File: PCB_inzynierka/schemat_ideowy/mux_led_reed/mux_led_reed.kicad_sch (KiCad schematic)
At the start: 70 parts, among them J1 Conn_01x01_Pin, J2 Conn_01x03_Pin, J3 Conn_01x01_Pin, J4 Conn_01x03_Pin, SW1 SW_Reed, SW10 SW_Reed, SW11 SW_Reed, SW12 SW_Reed, SW13 SW_Reed, SW14 SW_Reed, SW15 SW_Reed, SW16 SW_Reed, SW2 SW_Reed, SW3 SW_Reed, SW4 SW_Reed, SW5 SW_Reed, SW6 SW_Reed, SW7 SW_Reed, SW8 SW_Reed, SW9 SW_Reed, U1 74HC4051D_653, U2 74HC4051D_653

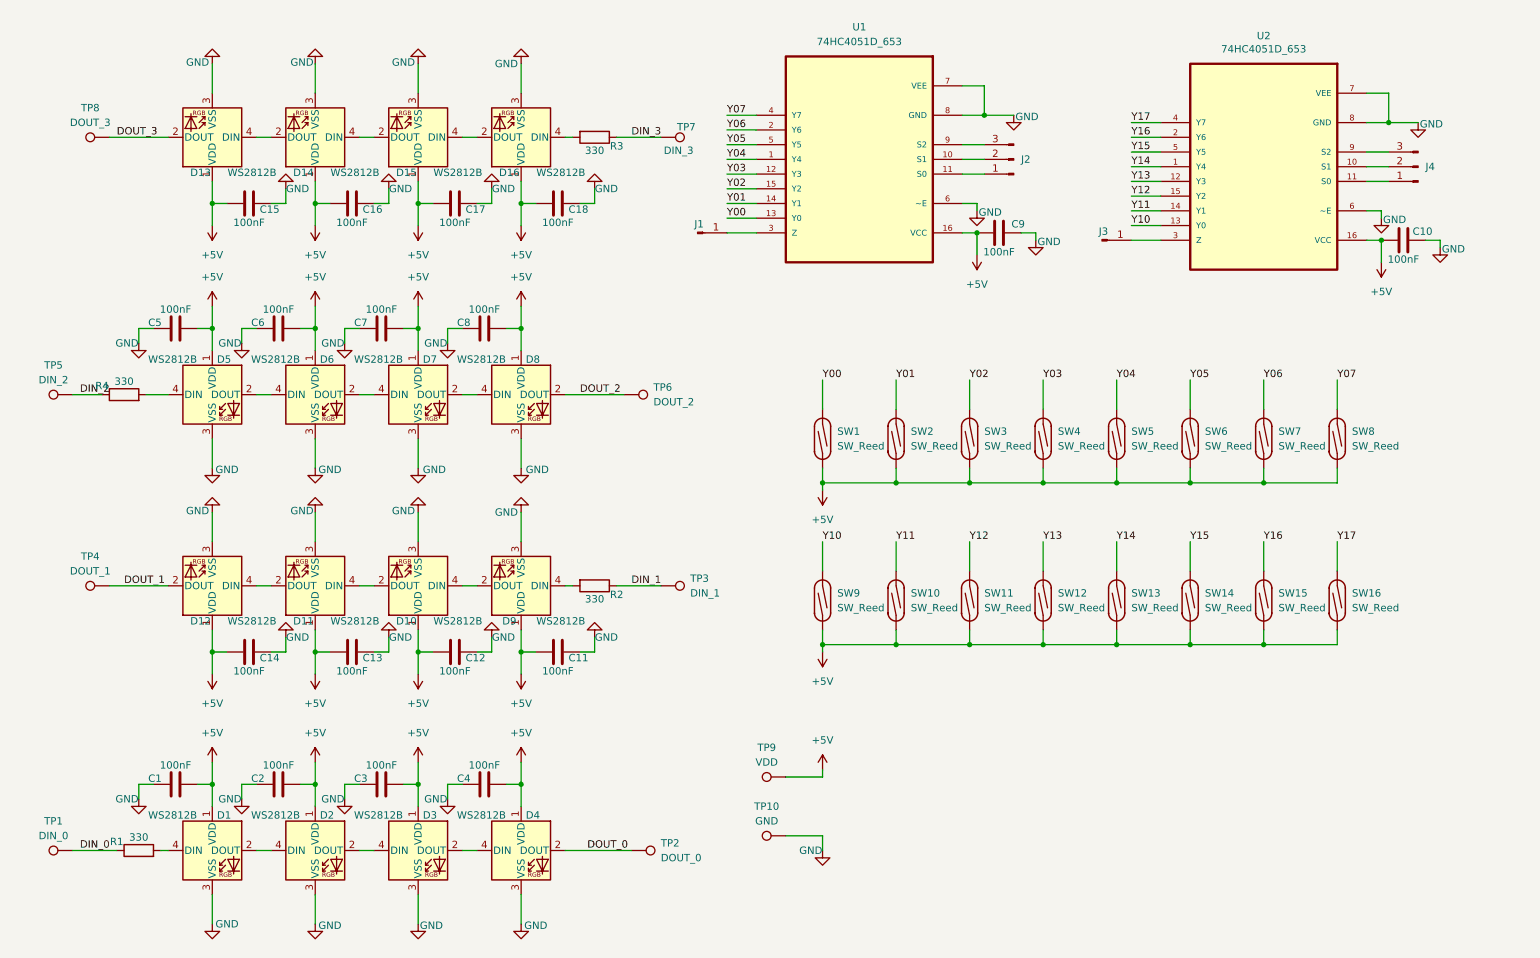
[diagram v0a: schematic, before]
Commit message: first version of 4x4 pcb for chessboard
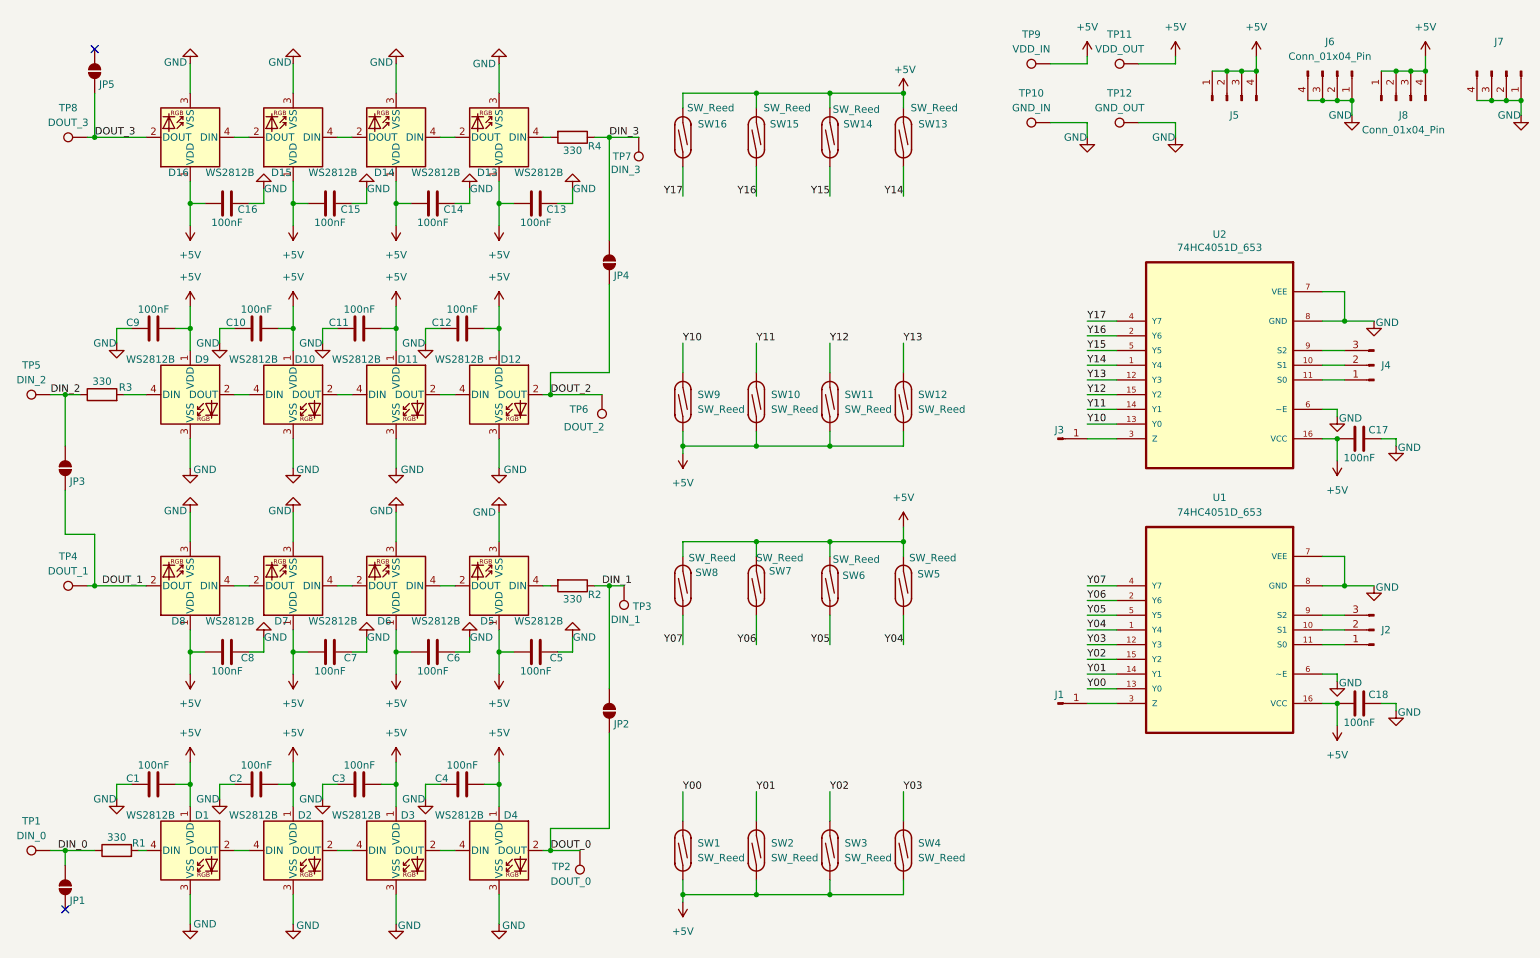
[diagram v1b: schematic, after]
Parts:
- added J5, J6: Conn_01x04_Pin, Connector_PinHeader_2.54mm:PinHeader_1x04_P2.54mm_Horizontal, symbol Connector:Conn_01x04_Pin
- added J7, J8: Conn_01x04_Pin, Connector_PinSocket_2.54mm:PinSocket_1x04_P2.54mm_Horizontal, symbol Connector:Conn_01x04_Pin
- added JP1, JP2, JP3, JP4, JP5: SolderJumper_2_Open, Jumper:SolderJumper-2_P1.3mm_Open_Pad1.0x1.5mm, symbol Jumper:SolderJumper_2_Open
- added TP11: VDD_OUT, TestPoint:TestPoint_Pad_4.0x4.0mm, symbol Connector:TestPoint
- added TP12: GND_OUT, TestPoint:TestPoint_Pad_4.0x4.0mm, symbol Connector:TestPoint
- J1, J3: footprint Connector_PinHeader_2.00mm:PinHeader_1x01_P2.00mm_Vertical -> Connector_PinHeader_2.54mm:PinHeader_1x01_P2.54mm_Vertical
- TP1, TP2, TP3, TP4, TP5, TP6, TP7, TP8: footprint TestPoint:TestPoint_Pad_4.0x4.0mm -> TestPoint:TestPoint_Pad_3.0x3.0mm
- TP10: value GND -> GND_IN
- TP9: value VDD -> VDD_IN
- renumbered C6 to C10, C7 to C11, C8 to C12, C18 to C13, C17 to C14, C16 to C15, C15 to C16, C10 to C17, C9 to C18, C11 to C5, C12 to C6, C13 to C7, C14 to C8, C5 to C9, D6 to D10, D7 to D11, D8 to D12, D16 to D13, D15 to D14, D14 to D15, D13 to D16, D9 to D5, D10 to D6, D11 to D7, D12 to D8, D5 to D9, R4 to R3, R3 to R4
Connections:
- net +5V: now also J5.1 (Pin_1), J5.2 (Pin_2), J5.3 (Pin_3), J5.4 (Pin_4), J8.1 (Pin_1), J8.2 (Pin_2), J8.3 (Pin_3), J8.4 (Pin_4), TP11.1
- net DIN_0: now also JP1.2 (B)
- net DIN_1: now also JP2.2 (B)
- net DIN_2: now also JP3.2 (B)
- net DIN_3: now also JP4.2 (B)
- net DOUT_0: now also JP2.1 (A)
- net DOUT_1: now also JP3.1 (A)
- net DOUT_2: now also JP4.1 (A)
- net DOUT_3: now also JP5.1 (A)
- net GND: now also J6.1 (Pin_1), J6.2 (Pin_2), J6.3 (Pin_3), J6.4 (Pin_4), J7.1 (Pin_1), J7.2 (Pin_2), J7.3 (Pin_3), J7.4 (Pin_4), TP12.1
- no-connect marks 0 -> 2
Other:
- moved on the sheet: C1, C10, C11, C12, C13, C14, C15, C16, C17, C18, C2, C3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

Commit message: plytka 4x4 zawierajaca mux, reed switche i ledy argb v1.0
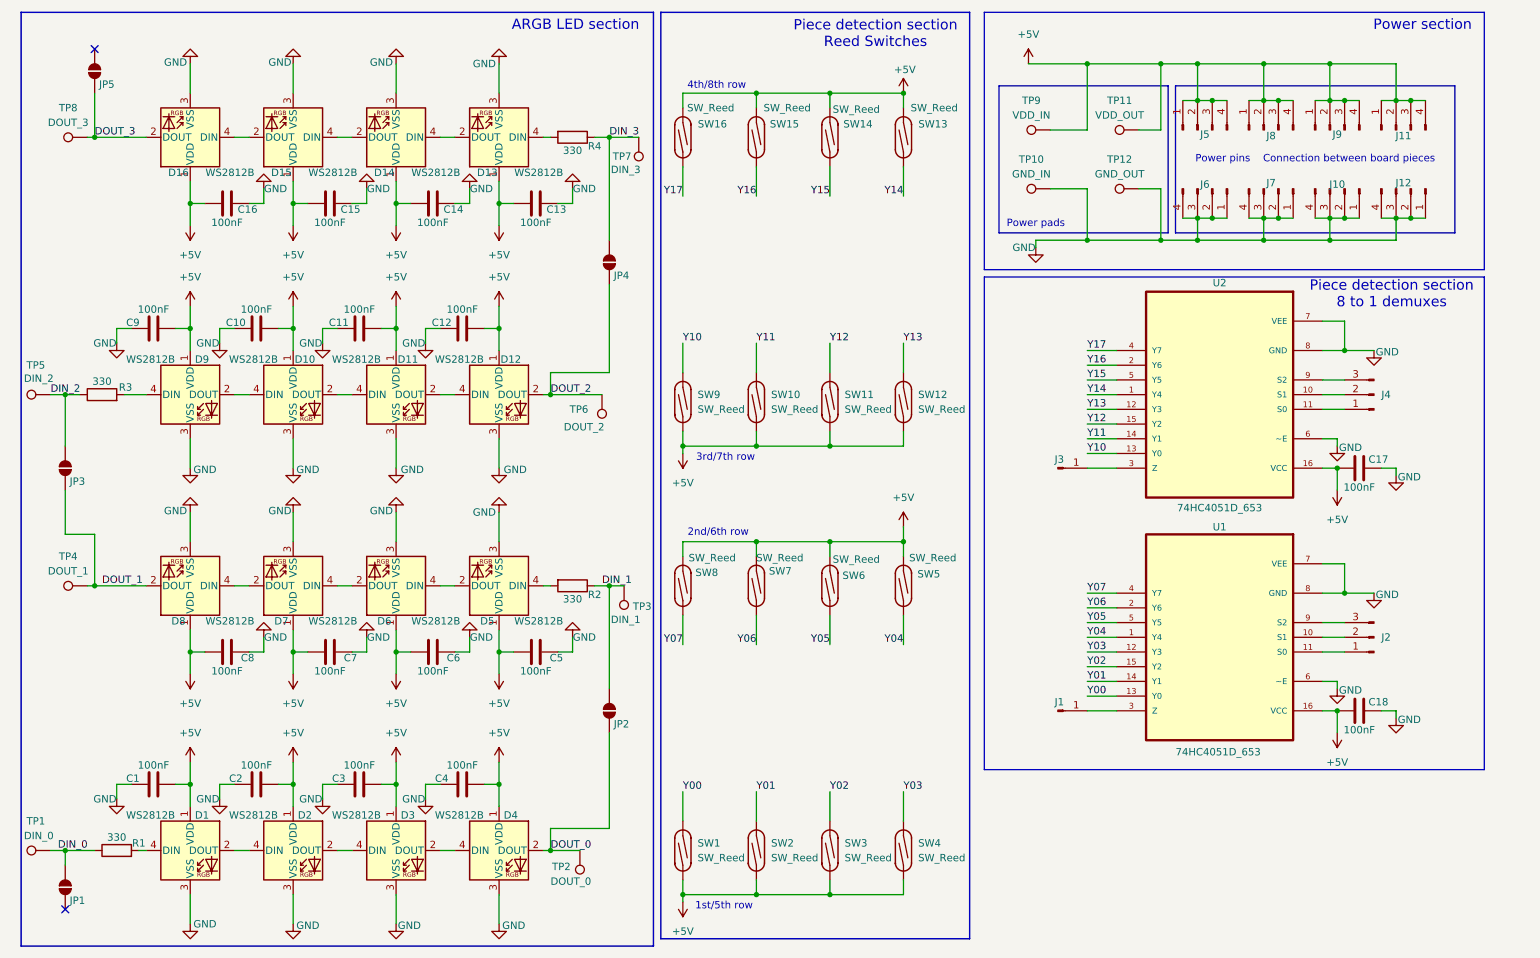
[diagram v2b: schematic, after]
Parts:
- added J10, J9: Conn_01x04_Pin, Connector_PinHeader_2.54mm:PinHeader_1x04_P2.54mm_Horizontal, symbol Connector:Conn_01x04_Pin
- added J11, J12: Conn_01x04_Pin, Connector_PinSocket_2.54mm:PinSocket_1x04_P2.54mm_Horizontal, symbol Connector:Conn_01x04_Pin
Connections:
- net +5V: now also J11.1 (Pin_1), J11.2 (Pin_2), J11.3 (Pin_3), J11.4 (Pin_4), J9.1 (Pin_1), J9.2 (Pin_2), J9.3 (Pin_3), J9.4 (Pin_4)
- net GND: now also J10.1 (Pin_1), J10.2 (Pin_2), J10.3 (Pin_3), J10.4 (Pin_4), J12.1 (Pin_1), J12.2 (Pin_2), J12.3 (Pin_3), J12.4 (Pin_4)
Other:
- note added: "1st/5th row"
- note added: "2nd/6th row"
- note added: "3rd/7th row"
- note added: "4th/8th row"
- note added: "ARGB LED section"
- note added: "Piece detection section 8 to 1 demuxes"
- note added: "Piece detection section Reed Switches"
- note added: "Power pads"
- note added: "Power pins Connection between board pieces"
- note added: "Power section"
- moved on the sheet: C17, C18, J1, J2, J3, J4, J5, J6, J7, J8, TP10, TP11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

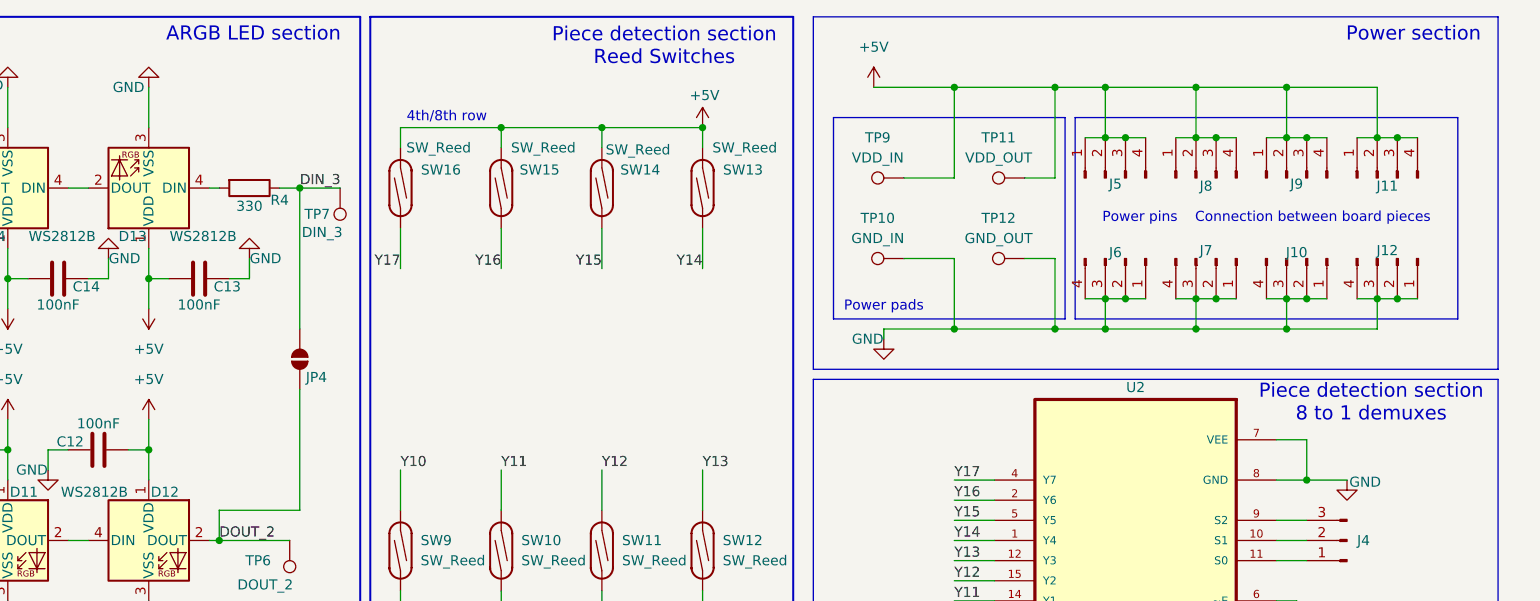
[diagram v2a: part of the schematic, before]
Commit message: obie plytki pcb przygotowane, schematy ideowe opisane
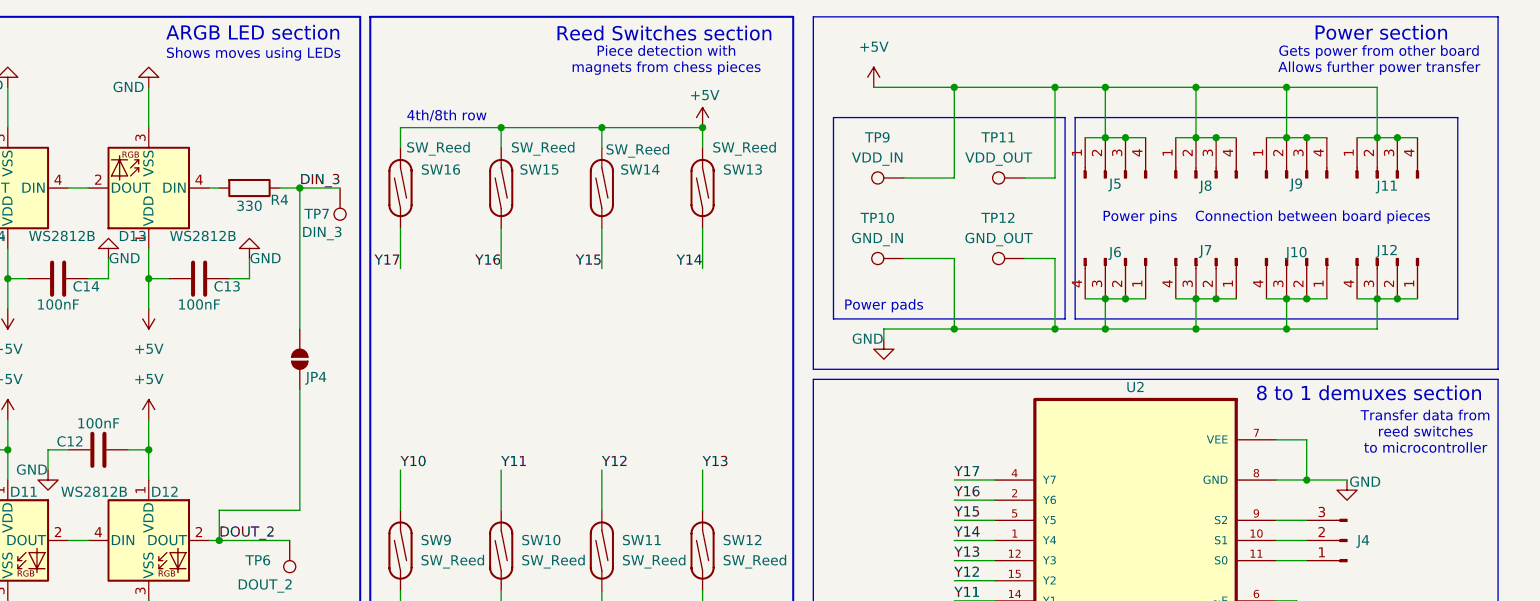
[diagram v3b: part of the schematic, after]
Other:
- note added: "8 to 1 demuxes section"
- note added: "Gets power from other board Allows further power transfer"
- note added: "Piece detection with magnets from chess pieces"
- note added: "Reed Switches section"
- note added: "Shows moves using LEDs"
- note added: "Transfer data from reed switches to microcontroller"
- note removed: "Piece detection section 8 to 1 demuxes"
- note removed: "Piece detection section Reed Switches"
- company: (none) -> AGH
- title: (none) -> 4x4 matryca led z kontaktronami i demultiplekserami
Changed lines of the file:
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@@
 	(generator_version "9.0")
 	(paper "A4")
+	(title_block
+		(title "4x4 matryca led z kontaktronami i demultiplekserami")
+		(date "2025-11-12")
+		(rev "1")
+		(company "AGH")
+		(comment 1 "Autor: Krystian Bajerski")
+		(comment 2 "Promotor: dr inż. Agnieszka Dąbrowska-Boruch")
+	)
 	(rectangle
 		(start 179.07 80.01)
@@
 		)
 	)
+	(text "Gets power from other board\nAllows further power transfer\n"
+		(exclude_from_sim no)
+		(at 250.444 39.878 0)
+		(effects
+			(font
+				(size 1.27 1.27)
+			)
+		)
+	)
 	(text "2nd/6th row"
 		(exclude_from_sim no)
 		(at 133.096 124.206 0)
+		(effects
+			(font
+				(size 1.27 1.27)
+			)
+		)
+	)
+	(text "Shows moves using LEDs"
+		(exclude_from_sim no)
+		(at 108.458 39.116 0)
 		(effects
 			(font
@@
 	(text "Power section\n"
 		(exclude_from_sim no)
-		(at 254.762 36.576 0)
+		(at 250.698 36.576 0)
 		(effects
 			(font
@@
 		)
 	)
-	(text "Piece detection section\n8 to 1 demuxes"
+	(text "8 to 1 demuxes section"
 		(exclude_from_sim no)
-		(at 249.428 83.058 0)
+		(at 249.174 82.042 0)
 		(effects
 			(font
@@
 		)
 	)
-	(text "Piece detection section\nReed Switches"
+	(text "Reed Switches section\n\n"
 		(exclude_from_sim no)
 		(at 160.274 38.1 0)
@@
 		)
 	)
+	(text "Piece detection with \nmagnets from chess pieces\n"
+		(exclude_from_sim no)
+		(at 160.528 39.878 0)
+		(effects
+			(font
+				(size 1.27 1.27)
+			)
+		)
+	)
 	(text "4th/8th row"
 		(exclude_from_sim no)
@@
 		(effects
 			(font
+				(size 1.27 1.27)
+			)
+		)
+	)
+	(text "Transfer data from \nreed switches\nto microcontroller"
+		(exclude_from_sim no)
+		(at 256.286 86.868 0)
+		(effects
+			(font
